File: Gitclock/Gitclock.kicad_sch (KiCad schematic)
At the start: 6 parts

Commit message: Week 2: Clock Schematic
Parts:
- removed D?: LED_0805, footprints:LED_0805_2012Metric, symbol HPS:LED_0805
- removed R?: R_0805_2.2K, footprints:R_0805_2012Metric, symbol HPS:R_0805_2.2K
- added C1, C?: C_0805_0.1uf, footprints:C_0805_2012Metric, symbol HPS:C_0805_0.1uf
- added J1: PJ-102AH, footprints:PJ-102AH, symbol HPS:PJ-102AH
- added J2: Conn_01x06, footprints:PinHeader_1x06_P2.54mm_Vertical, symbol HPS:Conn_01x06
- added U1: ATmega328-PU, footprints:DIP-28_W7.62mm, symbol HPS:ATmega328-PU
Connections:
- net GND: now also C1.2, C?.2, J1.2 (OUT), J2.1 (Pin_1), J2.2 (Pin_2), U1.8 (GND)
- new net: C1.1, J1.1 (POLE)
- new net: J2.4 (Pin_4), U1.2 (PD0)
- new net: J2.5 (Pin_5), U1.3 (PD1)
- new net: C?.1, U1.21 (AREF)

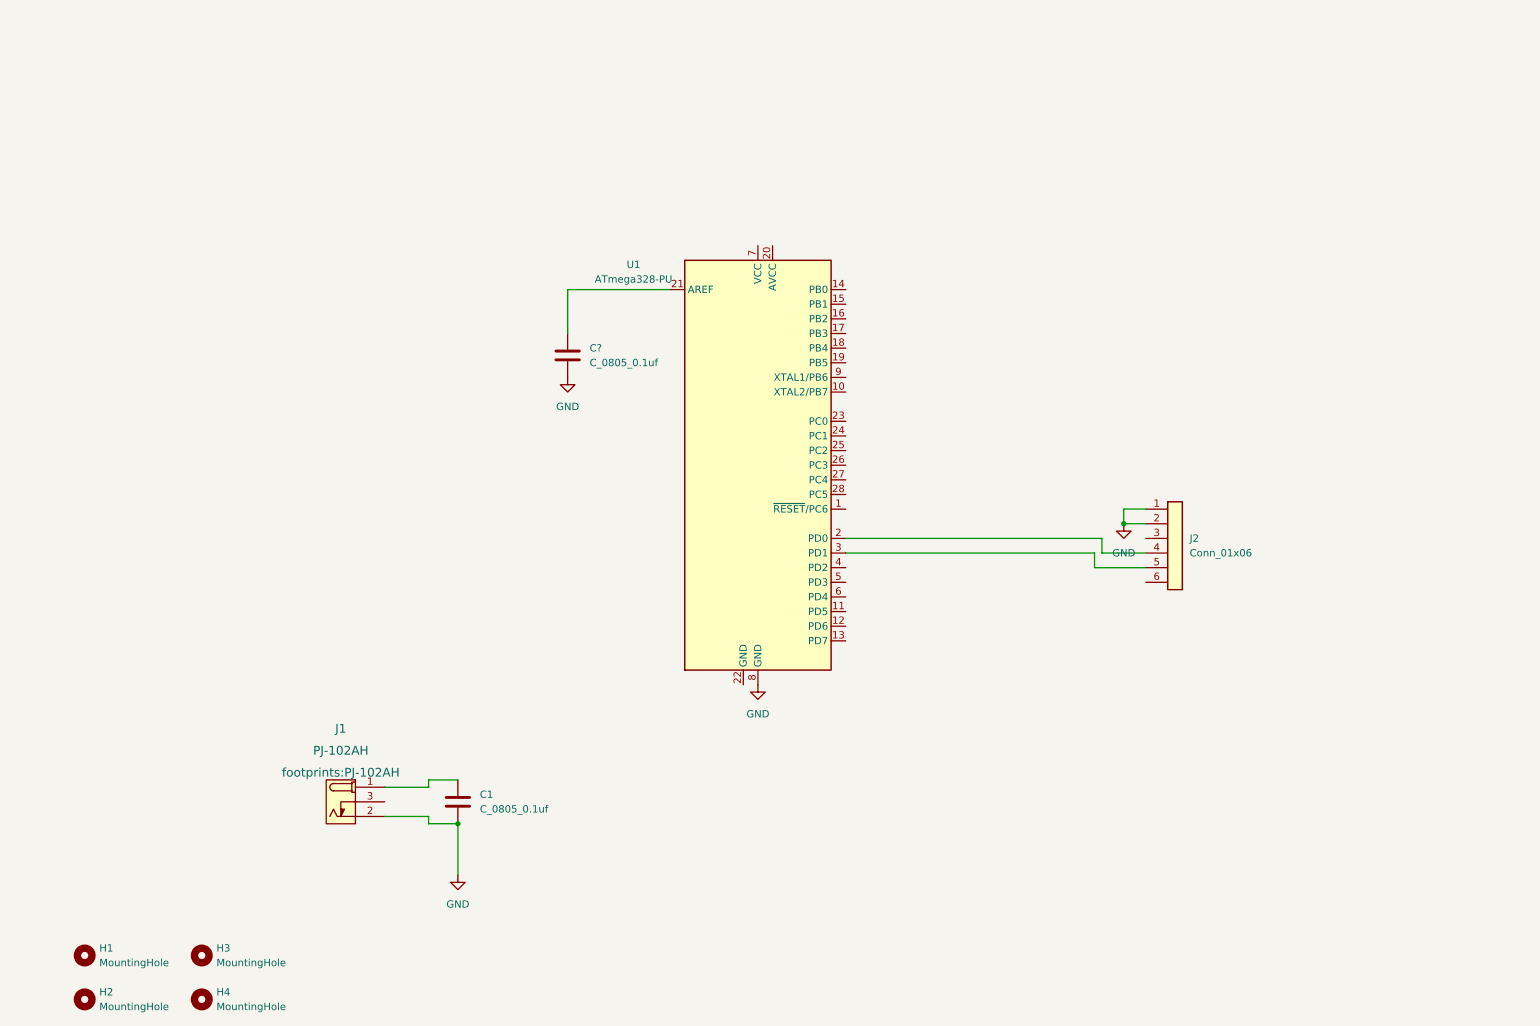
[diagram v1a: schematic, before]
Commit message: Switchcode
Button changes serial output from stating button is being pressed and not pressed
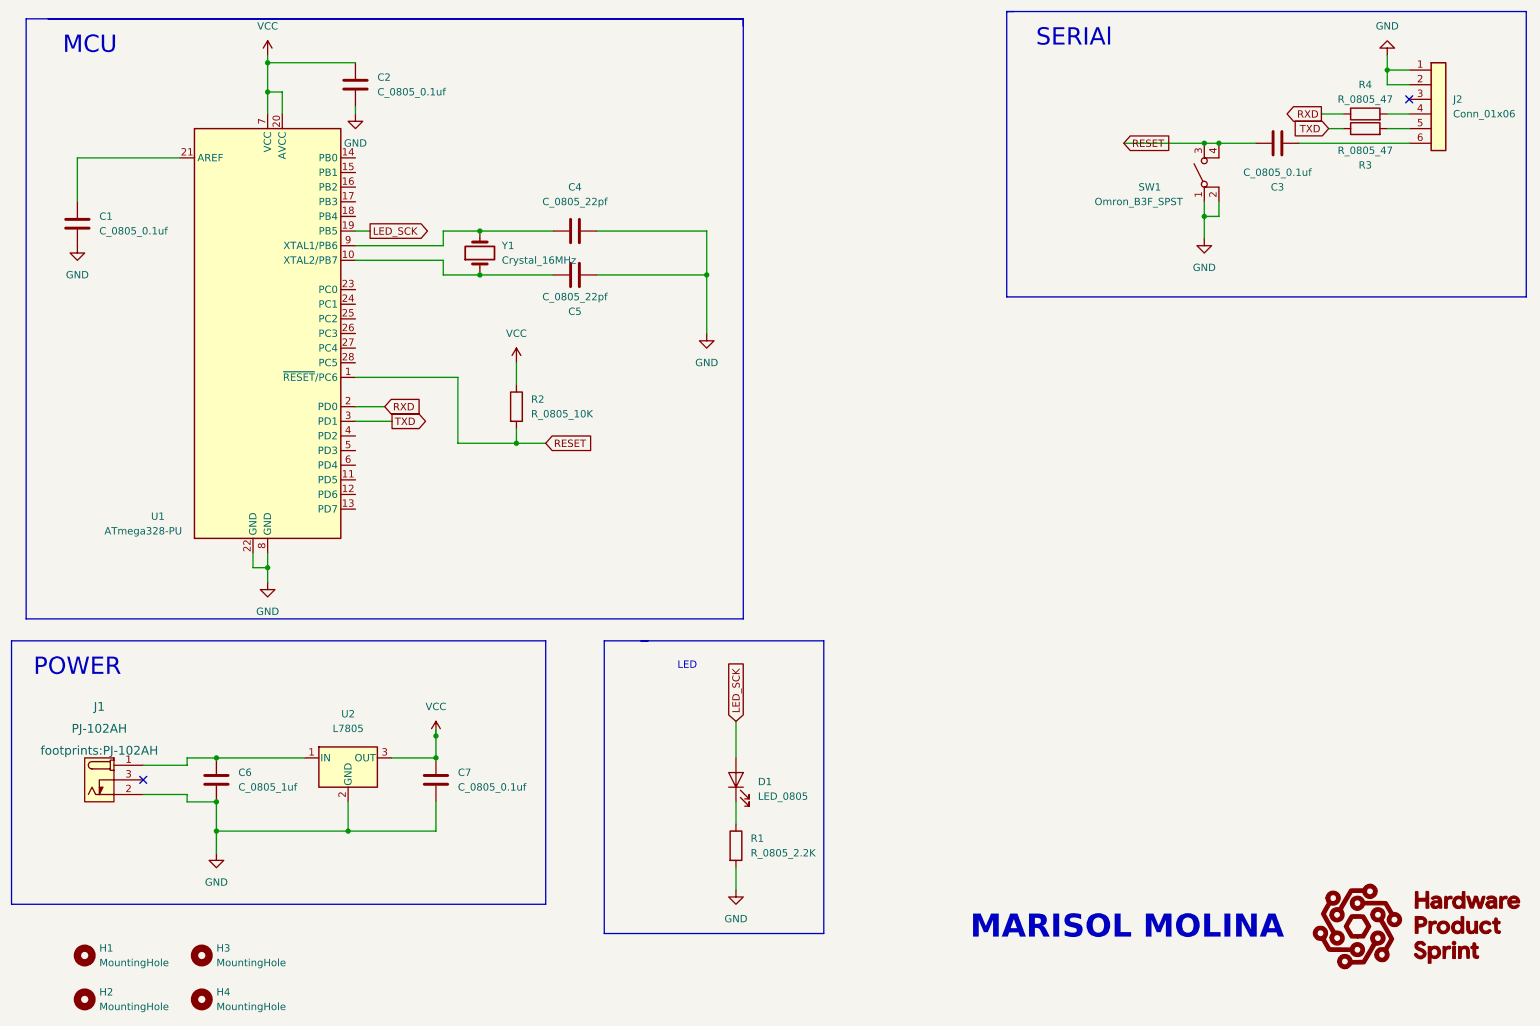
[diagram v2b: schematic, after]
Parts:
- removed C1: C_0805_0.1uf, footprints:C_0805_2012Metric, symbol HPS:C_0805_0.1uf
- added C2, C3, C7: C_0805_0.1uf, footprints:C_0805_2012Metric, symbol HPS:C_0805_0.1uf
- added C4, C5: C_0805_22pf, footprints:C_0805_2012Metric, symbol HPS:C_0805_22pf
- added C6: C_0805_1uf, footprints:C_0805_2012Metric, symbol HPS:C_0805_1uf
- added D1: LED_0805, footprints:LED_0805_2012Metric, symbol HPS:LED_0805
- added R1: R_0805_2.2K, footprints:R_0805_2012Metric, symbol HPS:R_0805_2.2K
- added R2: R_0805_10K, footprints:R_0805_2012Metric, symbol HPS:R_0805_10K
- added R3, R4: R_0805_47, footprints:R_0805_2012Metric, symbol HPS:R_0805_47
- added SW1: Omron_B3F_SPST, footprints:SW_SPST_Omron_B3FS-100xP, symbol HPS:Omron_B3F_SPST
- added U2: L7805, symbol HPS:L7805
- added Y1: Crystal_16MHz, footprints:Crystal_SMD_HC49-SD, symbol HPS:Crystal_16MHz
- gave numbers to parts that had none: 1
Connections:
- net GND: now also U1.22 (GND), C2.2, C4.2, C5.2, C6.2, C7.2, R1.2, SW1.1 (A), SW1.2 (A), U2.2 (GND)
- net at J1.1 (POLE): now also C6.1, U2.1 (IN)
- net at J2.4 (Pin_4): now also R4.2; no longer U1.2 (PD0)
- net at J2.5 (Pin_5): now also R3.2; no longer U1.3 (PD1)
- net at J2.6 (Pin_6): now also C3.2
- net RESET: now reaches U1.1 (~{RESET}/PC6)
- net RESET: now also C3.1, R2.2, SW1.3 (B), SW1.4 (B)
- net at U1.10 (XTAL2/PB7): now also C5.1, Y1.1
- net LED_SCK: now reaches U1.19 (PB5)
- net LED_SCK: now also D1.2 (A)
- net VCC: now reaches U1.20 (AVCC)
- net VCC: now also U1.7 (VCC), C2.1, C7.1, R2.1, U2.3 (OUT)
- net at U1.9 (XTAL1/PB6): now also C4.1, Y1.2
- new net: D1.1 (K), R1.1
- new net RXD: R4.1, U1.2 (PD0)
- new net TXD: R3.1, U1.3 (PD1)
- no-connect marks 0 -> 2
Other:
- note added: "LED"
- note added: "MARISOL MOLINA"
- note added: "MCU"
- note added: "POWER"
- note added: "SERIAl"
- moved on the sheet: C1, J1, J2, U1

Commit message: Update Gitclock
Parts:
- added BZ?: Buzzer, footprints:Buzzer_TDK_PS1240P02BT_D12.2mm_H6.5mm, symbol HPS:Buzzer
- added DS?: LED_Display_1001, footprints:Adafruit-1001-0-0-MFG, symbol HPS:LED_Display_1001
- added J?: Conn_01x05, footprints:PinHeader_1x05_P2.54mm_Vertical, symbol HPS:Conn_01x05
- added R? (x4): R_0805_10K, footprints:R_0805_2012Metric, symbol HPS:R_0805_10K
- added R? (x2): R_0805_1K, footprints:R_0805_2012Metric, symbol HPS:R_0805_1K
- added RV? (x3): R_POT_10K, footprints:Potentiometer_Bourns_3386P_Vertical, symbol HPS:R_POT_10K
- added SW? (x2): Omron_B3F_SPST, footprints:SW_SPST_Omron_B3FS-100xP, symbol HPS:Omron_B3F_SPST
- added U?: DS1307_DIP-8, footprints:DIP-8_W7.62mm, symbol HPS:DS1307_DIP-8
- added U?: WH2004A-CFH-JT#, footprints:WH2004A-CFH-JT#, symbol HPS:WH2004A-CFH-JT#
- added U?: MAX7219, footprints:DIP-24_W7.62mm, symbol HPS:MAX7219
- added Y?: Crystal_32768Hz, footprints:Crystal_SMD_2Pin_3.2x1.5mm, symbol HPS:Crystal_32768Hz
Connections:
- net GND: now also BZ?.1 (-), J?.1 (Pin_1), R?.2, R?.2, RV?.1, RV?.3, U?.1 (VSS), U?.16 (R), U?.4 (GND), U?.4 (GND), U?.5 (R/W), U?.9 (GND)
- net VCC: now also J?.2 (Pin_2), R?.1, R?.1, R?.2, RV?.1, RV?.2, RV?.3, SW?.1 (A), SW?.1 (A), U?.19 (V+), U?.2 (VDD), U?.8 (VCC)
- net at U1.11 (PD5): now also U?.11 (DB4)
- net at U1.12 (PD6): now also R?.2
- net at U1.13 (PD7): now also R?.1, SW?.3 (B)
- net at U1.14 (PB0): now also R?.1, SW?.3 (B)
- net FAN: now reaches U1.15 (PB1)
- net FAN: now also J?.4 (Pin_4)
- net SS: now reaches U1.16 (PB2)
- net SS: now also U?.12 (LOAD)
- net MOSI: now reaches U1.17 (PB3)
- net MOSI: now also U?.1 (DIN), U?.6 (E)
- net at U1.18 (PB4): now also U?.4 (RS)
- net at U1.24 (PC1): now also RV?.1
- net SDA: now reaches U1.27 (PC4)
- net SDA: now also R?.2, U?.5 (SDA)
- net SCL: now reaches U1.28 (PC5)
- net SCL: now also R?.2, U?.6 (SCL)
- net at U1.4 (PD2): now also U?.14 (DB7)
- net at U1.5 (PD3): now also U?.13 (DB6)
- net at U1.6 (PD4): now also U?.12 (DB5)
- net LED_SCK renamed SCK
- net SCK: now also U?.13 (CLK)
- new net: U?.1 (X1), Y?.1
- new net: U?.2 (X2), Y?.2
- new net: BZ?.2 (+), R?.1
- new net: DS?.1 (E), U?.21 (SEG_E)
- new net: DS?.10 (COM_DIG.3), U?.7 (DIG_3)
- new net: DS?.11 (COM_DIG.2), U?.6 (DIG_2)
- new net: DS?.12 (F), U?.15 (SEG_F)
- new net: DS?.13 (A), U?.14 (SEG_A)
- new net: DS?.14 (COM_DIG.1), U?.11 (DIG_1)
- new net: DS?.2 (D), U?.23 (SEG_D)
- new net: DS?.3 (DP), U?.22 (SEG_DP)
- new net: DS?.4 (C), U?.20 (SEG_C)
- new net: DS?.5 (G), U?.17 (SEG_G)
- new net: DS?.6 (COM_DIG.4), U?.3 (DIG_4)
- new net: DS?.9 (B), U?.16 (SEG_B)
- new net: RV?.2, U?.3 (VO)
- new net: R?.1, U?.15 (A)
- new net: RV?.3, U?.18 (ISET)
- new net +BATT: U?.3 (VBAT)
- no-connect marks 2 -> 13
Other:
- note added: "4 7 Segment Display"
- note added: "FAN"
- note added: "LCD Display"
- note added: "RTS"
- note added: "SETTINGS"
- note added: "SNOOZE"
- moved on the sheet: C1, C2, C3, C4, C5, C6, C7, D1, H1, H2, H3, H4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

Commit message: Updatedclock
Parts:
- gave numbers to parts that had none: 18

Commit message: gitclock
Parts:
- added R11: R_0805_10K, footprints:R_0805_2012Metric, symbol HPS:R_0805_10K
- added SW4: Omron_B3F_SPST, footprints:SW_SPST_Omron_B3FS-100xP, symbol HPS:Omron_B3F_SPST
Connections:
- net FAN: no longer U1.15 (PB1)
- net GND: now also R11.1
- net VCC: now also SW4.3 (B)
- new net: R11.2, SW4.1 (A), U1.15 (PB1)
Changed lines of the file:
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@@
   (junction (at 256.54 116.84) (diameter 0) (color 0 0 0 0)
+  )
+  (junction (at 203.2 99.06) (diameter 0) (color 0 0 0 0)
   )
   (no_connect (at 210.82 31.75))
@@
     (stroke (width 0) (type default) (color 0 0 0 0))
   )
+  (wire (pts (xy 207.01 99.06) (xy 207.01 97.79))
+    (stroke (width 0) (type default) (color 0 0 0 0))
+  )
   (wire (pts (xy 25.4 160.02) (xy 29.21 160.02))
     (stroke (width 0) (type default) (color 0 0 0 0))
@@
     (stroke (width 0) (type default) (color 0 0 0 0))
   )
+  (wire (pts (xy 203.2 99.06) (xy 207.01 99.06))
+    (stroke (width 0) (type default) (color 0 0 0 0))
+  )
   (wire (pts (xy 266.7 114.3) (xy 269.24 114.3))
     (stroke (width 0) (type default) (color 0 0 0 0))
@@
     (stroke (width 0) (type default) (color 0 0 0 0))
   )
-  (wire (pts (xy 195.58 99.06) (xy 201.93 99.06))
+  (wire (pts (xy 195.58 99.06) (xy 203.2 99.06))
     (stroke (width 0) (type default) (color 0 0 0 0))
   )
@@
   (text "MCU" (at 144.78 78.74 0)
     (effects (font (size 3 3)) (justify left bottom))
+  )
+  (text "FAN" (at 214.63 92.71 0)
+    (effects (font (size 1.27 1.27)) (justify left bottom))
   )
   (text "RTS\n" (at 237.49 20.32 0)
@@
     (effects (font (size 1.27 1.27)) (justify left))
     (property "Intersheet References" "${INTERSHEET_REFS}" (id 0) (at 169.4483 39.2906 0)
-      (effects (font (size 1.27 1.27)) (justify left) hide)
-    )
-  )
-  (global_label "FAN" (shape output) (at 201.93 99.06 0) (fields_autoplaced)
-    (effects (font (size 1.27 1.27)) (justify left))
-    (property "Intersheet References" "${INTERSHEET_REFS}" (id 0) (at 207.8507 98.9806 0)
       (effects (font (size 1.27 1.27)) (justify left) hide)
     )
@@
     )
     (property "Tolerance" "N/A" (id 10) (at 207.01 39.37 0)
+      (effects (font (size 1.27 1.27)) hide)
+    )
+    (pin "1")
+    (pin "2")
+  )
+  (symbol (lib_id "HPS:R_0805_10K") (at 203.2 95.25 0) (unit 1)
+    (in_bom yes) (on_board yes) (fields_autoplaced)
+    (property "Reference" "R11" (id 0) (at 205.74 93.9799 0)
+      (effects (font (size 1.27 1.27)) (justify left))
+    )
+    (property "Value" "R_0805_10K" (id 1) (at 205.74 96.5199 0)
+      (effects (font (size 1.27 1.27)) (justify left))
+    )
+    (property "Footprint" "footprints:R_0805_2012Metric" (id 2) (at 203.2 111.76 0)
+      (effects (font (size 1.27 1.27)) hide)
+    )
+    (property "Datasheet" "https://www.digikey.com/en/products/detail/yageo/RC0805FR-0710KL/727535" (id 3) (at 200.66 95.25 0)
+      (effects (font (size 1.27 1.27)) hide)
+    )
+    (property "MFG" "Yageo" (id 4) (at 203.2 106.68 0)
+      (effects (font (size 1.27 1.27)) hide)
+    )
+    (property "MPN" "RC0805FR-0710KL" (id 5) (at 203.2 109.22 0)
+      (effects (font (size 1.27 1.27)) hide)
+    )
+    (property "Digikey PN" "311-10.0KCRCT-ND" (id 6) (at 203.2 114.3 0)
+      (effects (font (size 1.27 1.27)) hide)
+    )
+    (property "Mouser PN" "N/A" (id 7) (at 203.2 116.84 0)
+      (effects (font (size 1.27 1.27)) hide)
+    )
+    (property "Power" "N/A" (id 8) (at 203.2 119.38 0)
+      (effects (font (size 1.27 1.27)) hide)
+    )
+    (property "Tolerance" "N/A" (id 9) (at 203.2 121.92 0)
       (effects (font (size 1.27 1.27)) hide)
     )
@@
     (pin "1")
     (pin "2")
+  )
+  (symbol (lib_id "HPS:Omron_B3F_SPST") (at 212.09 97.79 0) (unit 1)
+    (in_bom yes) (on_board yes) (fields_autoplaced)
+    (property "Reference" "SW4" (id 0) (at 212.09 91.44 0))
+    (property "Value" "Omron_B3F_SPST" (id 1) (at 212.09 93.98 0))
+    (property "Footprint" "footprints:SW_SPST_Omron_B3FS-100xP" (id 2) (at 212.09 109.22 0)
+      (effects (font (size 1.27 1.27)) hide)
+    )
+    (property "Datasheet" "https://omronfs.omron.com/en_US/ecb/products/pdf/en-b3fs.pdf" (id 3) (at 212.09 97.79 0)
+      (effects (font (size 1.27 1.27)) hide)
+    )
+    (property "MFG" "Omron Electronics Inc-EMC Div" (id 4) (at 212.09 104.14 0)
+      (effects (font (size 1.27 1.27)) hide)
+    )
+    (property "MPN" "B3FS-1000P" (id 5) (at 212.09 106.68 0)
+      (effects (font (size 1.27 1.27)) hide)
+    )
+    (property "Digikey PN" "SW423CT-ND" (id 6) (at 212.09 111.76 0)
+      (effects (font (size 1.27 1.27)) hide)
+    )
+    (property "Mouser PN" "N/A" (id 7) (at 212.09 114.3 0)
+      (effects (font (size 1.27 1.27)) hide)
+    )
+    (pin "1")
+    (pin "2")
+    (pin "3")
+    (pin "4")
   )
   (symbol (lib_id "HPS:Conn_01x05") (at 20.32 162.56 180) (unit 1)
@@
     )
   )
+  (symbol (lib_id "HPS:GND") (at 203.2 91.44 180) (unit 1)
+    (in_bom yes) (on_board yes) (fields_autoplaced)
+    (property "Reference" "#PWR026" (id 0) (at 203.2 85.09 0)
+      (effects (font (size 1.27 1.27)) hide)
+    )
+    (property "Value" "GND" (id 1) (at 203.2 86.36 0))
+    (property "Footprint" "" (id 2) (at 203.2 91.44 0)
+      (effects (font (size 1.27 1.27)) hide)
+    )
+    (property "Datasheet" "" (id 3) (at 203.2 91.44 0)
+      (effects (font (size 1.27 1.27)) hide)
+    )
+    (pin "1")
+  )
   (symbol (lib_id "HPS:VCC") (at 223.52 132.08 0) (unit 1)
     (in_bom yes) (on_board yes) (fields_autoplaced)
@@
     (pin "2")
   )
+  (symbol (lib_id "HPS:VCC") (at 217.17 97.79 270) (unit 1)
+    (in_bom yes) (on_board yes) (fields_autoplaced)
+    (property "Reference" "#PWR027" (id 0) (at 213.36 97.79 0)
+      (effects (font (size 1.27 1.27)) hide)
+    )
+    (property "Value" "VCC" (id 1) (at 220.98 97.7899 90)
+      (effects (font (size 1.27 1.27)) (justify left))
+    )
+    (property "Footprint" "" (id 2) (at 217.17 97.79 0)
+      (effects (font (size 1.27 1.27)) hide)
+    )
+    (property "Datasheet" "" (id 3) (at 217.17 97.79 0)
+      (effects (font (size 1.27 1.27)) hide)
+    )
+    (pin "1")
+  )
   (symbol (lib_id "HPS:GND") (at 165.1 146.05 0) (unit 1)
     (in_bom yes) (on_board yes) (fields_autoplaced)
@@
       (reference "#PWR025") (unit 1) (value "VCC") (footprint "")
     )
+    (path "/b2f7aa7c-1b8a-4b2a-b447-22be93212478"
+      (reference "#PWR026") (unit 1) (value "GND") (footprint "")
+    )
+    (path "/fcda8e25-b4ca-4300-bca3-4f296e33f7cc"
+      (reference "#PWR027") (unit 1) (value "VCC") (footprint "")
+    )
     (path "/b8ab70f2-d09f-4473-ad37-89ea941dca60"
       (reference "BZ1") (unit 1) (value "Buzzer") (footprint "footprints:Buzzer_TDK_PS1240P02BT_D12.2mm_H6.5mm")
@@
       (reference "R10") (unit 1) (value "R_0805_1K") (footprint "footprints:R_0805_2012Metric")
     )
+    (path "/17ccefeb-a492-427b-8efd-13f0e4786ae3"
+      (reference "R11") (unit 1) (value "R_0805_10K") (footprint "footprints:R_0805_2012Metric")
+    )
     (path "/99c06508-6a16-489f-a186-ced706cf79b5"
       (reference "RV1") (unit 1) (value "R_POT_10K") (footprint "footprints:Potentiometer_Bourns_3386P_Vertical")
@@
       (reference "SW3") (unit 1) (value "Omron_B3F_SPST") (footprint "footprints:SW_SPST_Omron_B3FS-100xP")
     )
+    (path "/5f30d32f-818b-4e3a-9a53-1ff51ebb71a9"
+      (reference "SW4") (unit 1) (value "Omron_B3F_SPST") (footprint "footprints:SW_SPST_Omron_B3FS-100xP")
+    )
     (path "/69182d8d-4416-465a-9377-142ba3779f64"

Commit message: gitclock6302022
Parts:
- removed R10, R7: R_0805_1K, footprints:R_0805_2012Metric, symbol HPS:R_0805_1K
- removed RV2, RV3: R_POT_10K, footprints:Potentiometer_Bourns_3386P_Vertical, symbol HPS:R_POT_10K
- removed U5: WH2004A-CFH-JT#, footprints:WH2004A-CFH-JT#, symbol HPS:WH2004A-CFH-JT#
- added BT1: Battery_Cell, footprints:BatteryHolder_Keystone_106_1x20mm, symbol HPS:Battery_Cell
- added DS2: TC1602A-01T, footprints:TC1602A-01T, symbol HPS:TC1602A-01T
- added SW5: RotaryEncoder_Switch, footprints:RotaryEncoder_TT_EN11-Switch_Vertical_H20mm_CircularMountingHoles, symbol HPS:RotaryEncoder_Switch
- added U5: ULN2003A, footprints:DIP-16_W7.62mm, symbol HPS:ULN2003A
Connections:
- net +BATT: now also BT1.1 (+)
- net FAN: now also BZ1.2 (+), R11.2, SW4.1 (A), U1.15 (PB1); no longer J3.4 (Pin_4)
- net GND: now also BT1.2 (-), DS2.1 (VSS), DS2.16 (LED(-)), DS2.5 (R/W), SW5.C, U5.8 (GND)
- net MOSI: now also DS2.6 (E)
- net SCL: now also SW5.A
- net VCC: now also DS2.15 (LED(+)), DS2.2 (VDD), SW5.S1, U5.9 (COM); no longer SW4.3 (B)
- net SNOOZE: now reaches R6.1, SW2.3 (B), U1.14 (PB0)
- net BUZZER: now reaches U1.12 (PD6)
- net D7: now reaches U1.11 (PD5)
- net D7: now also DS2.14 (D7)
- net MENU: now reaches R5.1, SW3.3 (B), U1.13 (PD7)
- net RS: now reaches U1.18 (PB4)
- net RS: now also DS2.4 (RS)
- net MENU SCROLL: now reaches U1.24 (PC1)
- net MENU SCROLL: now also SW5.B
- net D4: now reaches U1.4 (PD2)
- net D4: now also DS2.11 (D4)
- net D5: now reaches U1.5 (PD3)
- net D5: now also DS2.12 (D5)
- net D6: now reaches U1.6 (PD4)
- net D6: now also DS2.13 (D6)
- new net: SW4.3 (B), U5.1 (I1)
- new net: J3.4 (Pin_4), U5.16 (O1)
- no-connect marks 13 -> 25
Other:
- note added: "BUZZER"
- note added: "MENU"
- note added: "MENU SCROLL"
- note removed: "SETTINGS"
- moved on the sheet: BZ1, C1, C2, C3, C4, C5, C6, C7, D1, DS1, H3, H4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

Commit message: Clock20220704
11:06 AM
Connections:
- net MENU SCROLL is gone; now on net GND: SW5.B, U1.24 (PC1)
- net GND: now also R5.1; no longer R5.2
- net MENU: now also R5.2; no longer R5.1
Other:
- moved on the sheet: BT1, R11, R5, R6, SW2, SW3
